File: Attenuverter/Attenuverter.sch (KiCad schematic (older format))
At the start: 53 parts

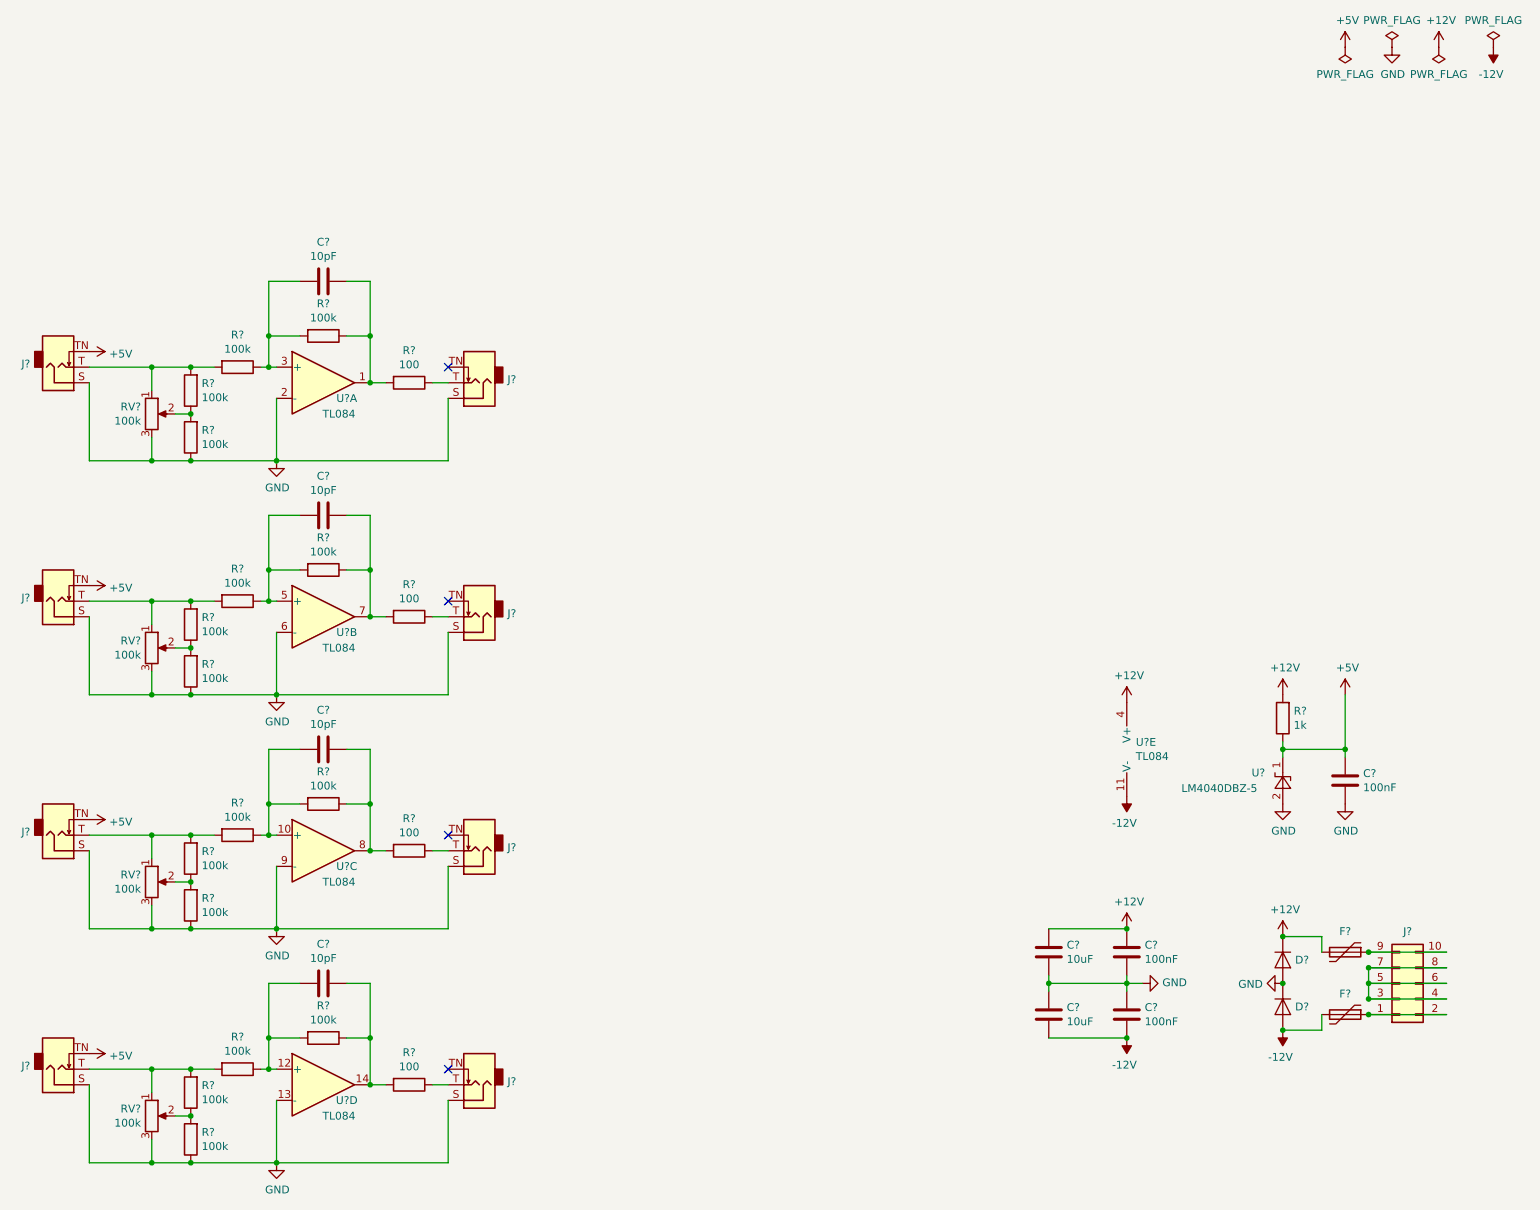
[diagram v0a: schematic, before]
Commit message: Assign footprints
Layout Components
Layout Board
Add Gnd Pours
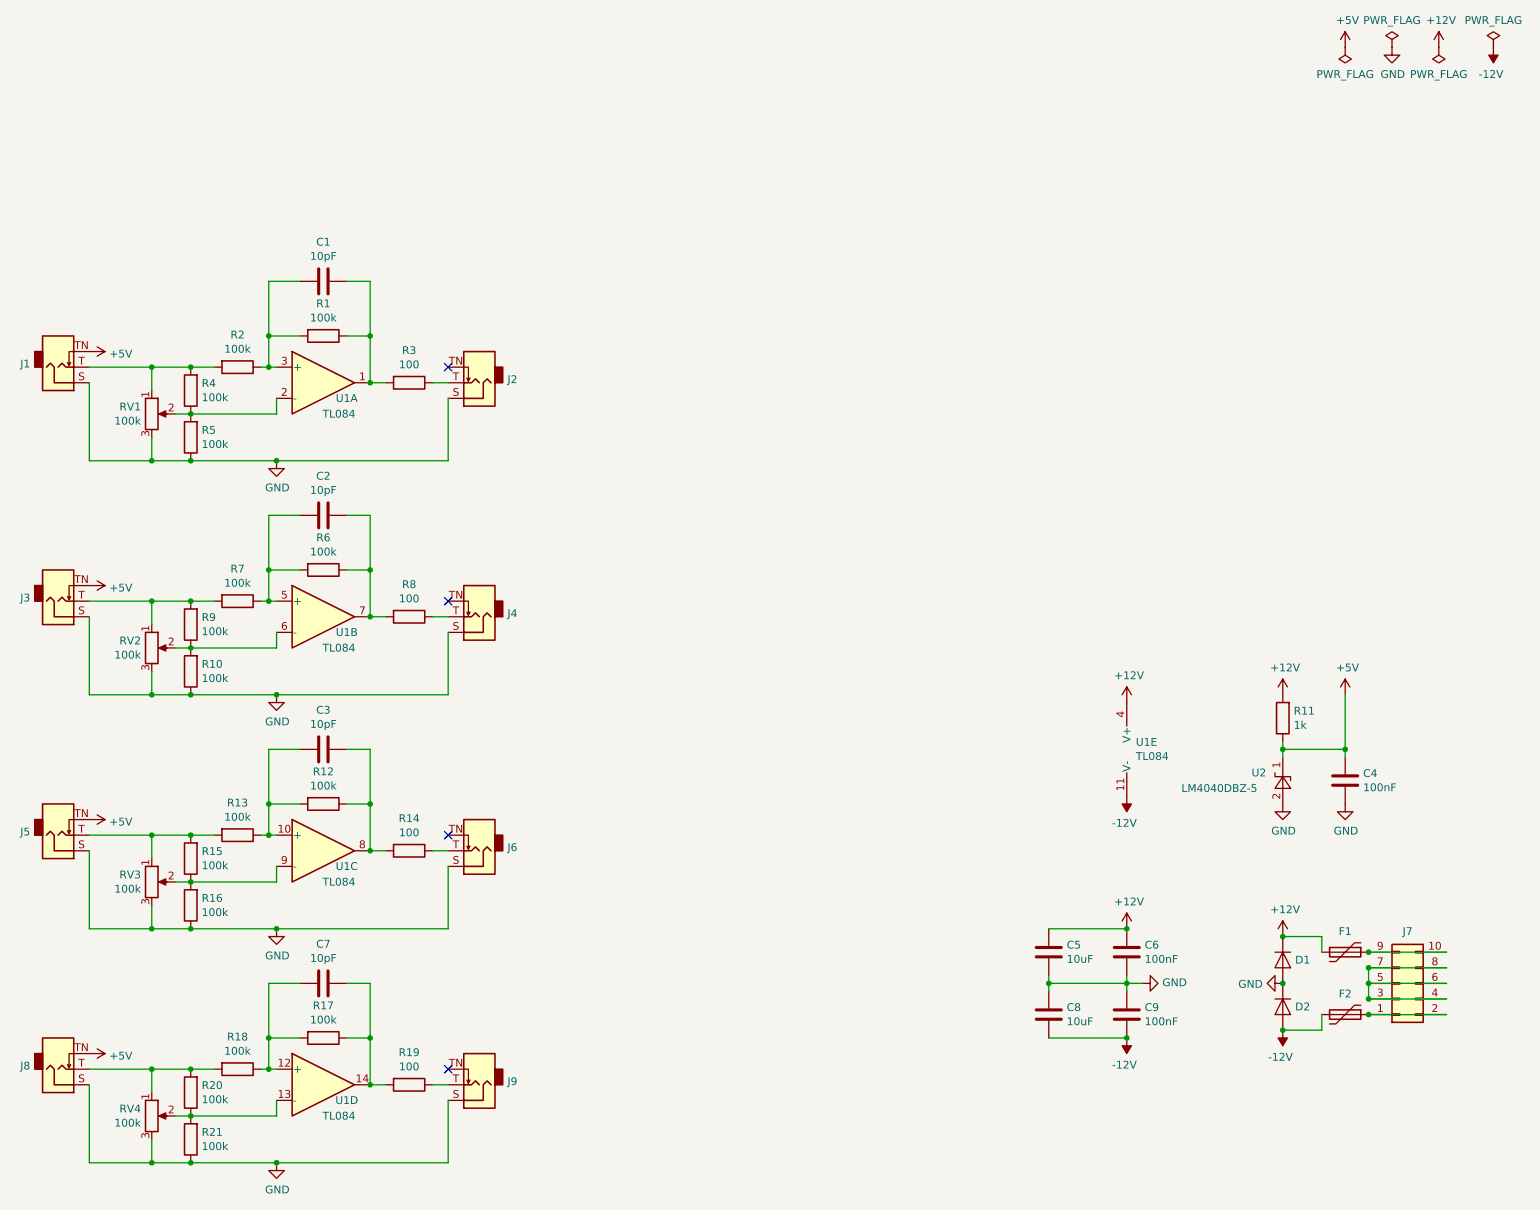
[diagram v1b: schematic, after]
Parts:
- C1, C2, C3, C4, C5, C6, C7, C8, C9: renamed from C?; footprint (none) -> Capacitors_SMD:C_0805_HandSoldering
- D1, D2: renamed from D?; footprint (none) -> Diodes_SMD:D_SMA_Handsoldering
- F1, F2: renamed from F?; footprint (none) -> Fuse_Holders_and_Fuses:Fuse_SMD1206_HandSoldering
- J1, J2, J3, J4, J5, J6, J8, J9: renamed from J?; footprint (none) -> _NTSFootprints:Jack_3.5mm_QingPu_WQP-PJ398SM_Vertical_CenterHole_OvalPads
- J7: renamed from J?; footprint (none) -> _NTSFootprints:PinHeader_2x05_P2.54mm_Vertical_Shrouded
- R1, R10, R11, R12, R13, R14, R15, R16, R17, R18, R19, R2, R20, R21, R3, R4, R5, R6, R7, R8, R9: renamed from R?; footprint (none) -> Resistors_SMD:R_0805_HandSoldering
- RV1, RV2, RV3, RV4: renamed from RV?; footprint (none) -> _NTSFootprints:Potentiometer_Alps_RK09L_Plated_Mount_Holes
- U1: renamed from U?; footprint (none) -> Housings_SOIC:SOIC-14_3.9x8.7mm_Pitch1.27mm
- U2: renamed from U?; footprint Package_TO_SOT_SMD:SOT-23 -> TO_SOT_Packages_SMD:SOT-23
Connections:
- net GND: no longer U1.13 (-), U1.2 (-), U1.6 (-), U1.9 (-)
- net at R4.1, R5.2, RV1.2: now also U1.2 (-)
- net at R10.2, R9.1, RV2.2: now also U1.6 (-)
- net at R15.1, R16.2, RV3.2: now also U1.9 (-)
- net at R20.1, R21.2, RV4.2: now also U1.13 (-)

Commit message: Finish routing
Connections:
- net GND: now also J7.3 (Pin_3), J7.4 (Pin_4), J7.5 (Pin_5), J7.6 (Pin_6), J7.7 (Pin_7), J7.8 (Pin_8)
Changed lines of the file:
@@
 Wire Wire Line
 	3050 1850 3050 1750
+Wire Wire Line
+	10050 5500 9500 5500
 $EndSCHEMATC

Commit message: Swap inverting and non inverting inputs.  Generate gerbers
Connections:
- net at R4.1, R5.2, RV1.2: now also U1.3 (+); no longer U1.2 (-)
- net at C1.2, R1.2, R2.1: now also U1.2 (-); no longer U1.3 (+)
- net at C2.2, R6.2, R7.1: now also U1.6 (-); no longer U1.5 (+)
- net at R10.2, R9.1, RV2.2: now also U1.5 (+); no longer U1.6 (-)
- net at C3.2, R12.2, R13.1: now also U1.9 (-); no longer U1.10 (+)
- net at R15.1, R16.2, RV3.2: now also U1.10 (+); no longer U1.9 (-)
- net at C7.2, R17.2, R18.1: now also U1.13 (-); no longer U1.12 (+)
- net at R20.1, R21.2, RV4.2: now also U1.12 (+); no longer U1.13 (-)
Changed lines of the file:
@@
 F 3 "http://www.ti.com/lit/ds/symlink/tl081.pdf" H 3400 1850 50  0001 C CNN
 	1    3350 1650
-	1    0    0    -1
+	1    0    0    1
 $EndComp
 $Comp
@@
 F 3 "http://www.ti.com/lit/ds/symlink/tl081.pdf" H 3400 3350 50  0001 C CNN
 	2    3350 3150
-	1    0    0    -1
+	1    0    0    1
 $EndComp
 $Comp
@@
 F 3 "http://www.ti.com/lit/ds/symlink/tl081.pdf" H 3400 4850 50  0001 C CNN
 	3    3350 4650
-	1    0    0    -1
+	1    0    0    1
 $EndComp
 $Comp
@@
 F 3 "http://www.ti.com/lit/ds/symlink/tl081.pdf" H 3400 6350 50  0001 C CNN
 	4    3350 6150
-	1    0    0    -1
-$EndComp
-$Comp
+	1    0    0    1
+$EndComp
+$Comp
